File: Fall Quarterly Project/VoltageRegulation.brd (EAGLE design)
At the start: 160 x 100 mm, 24 parts, among them IC3 L272M

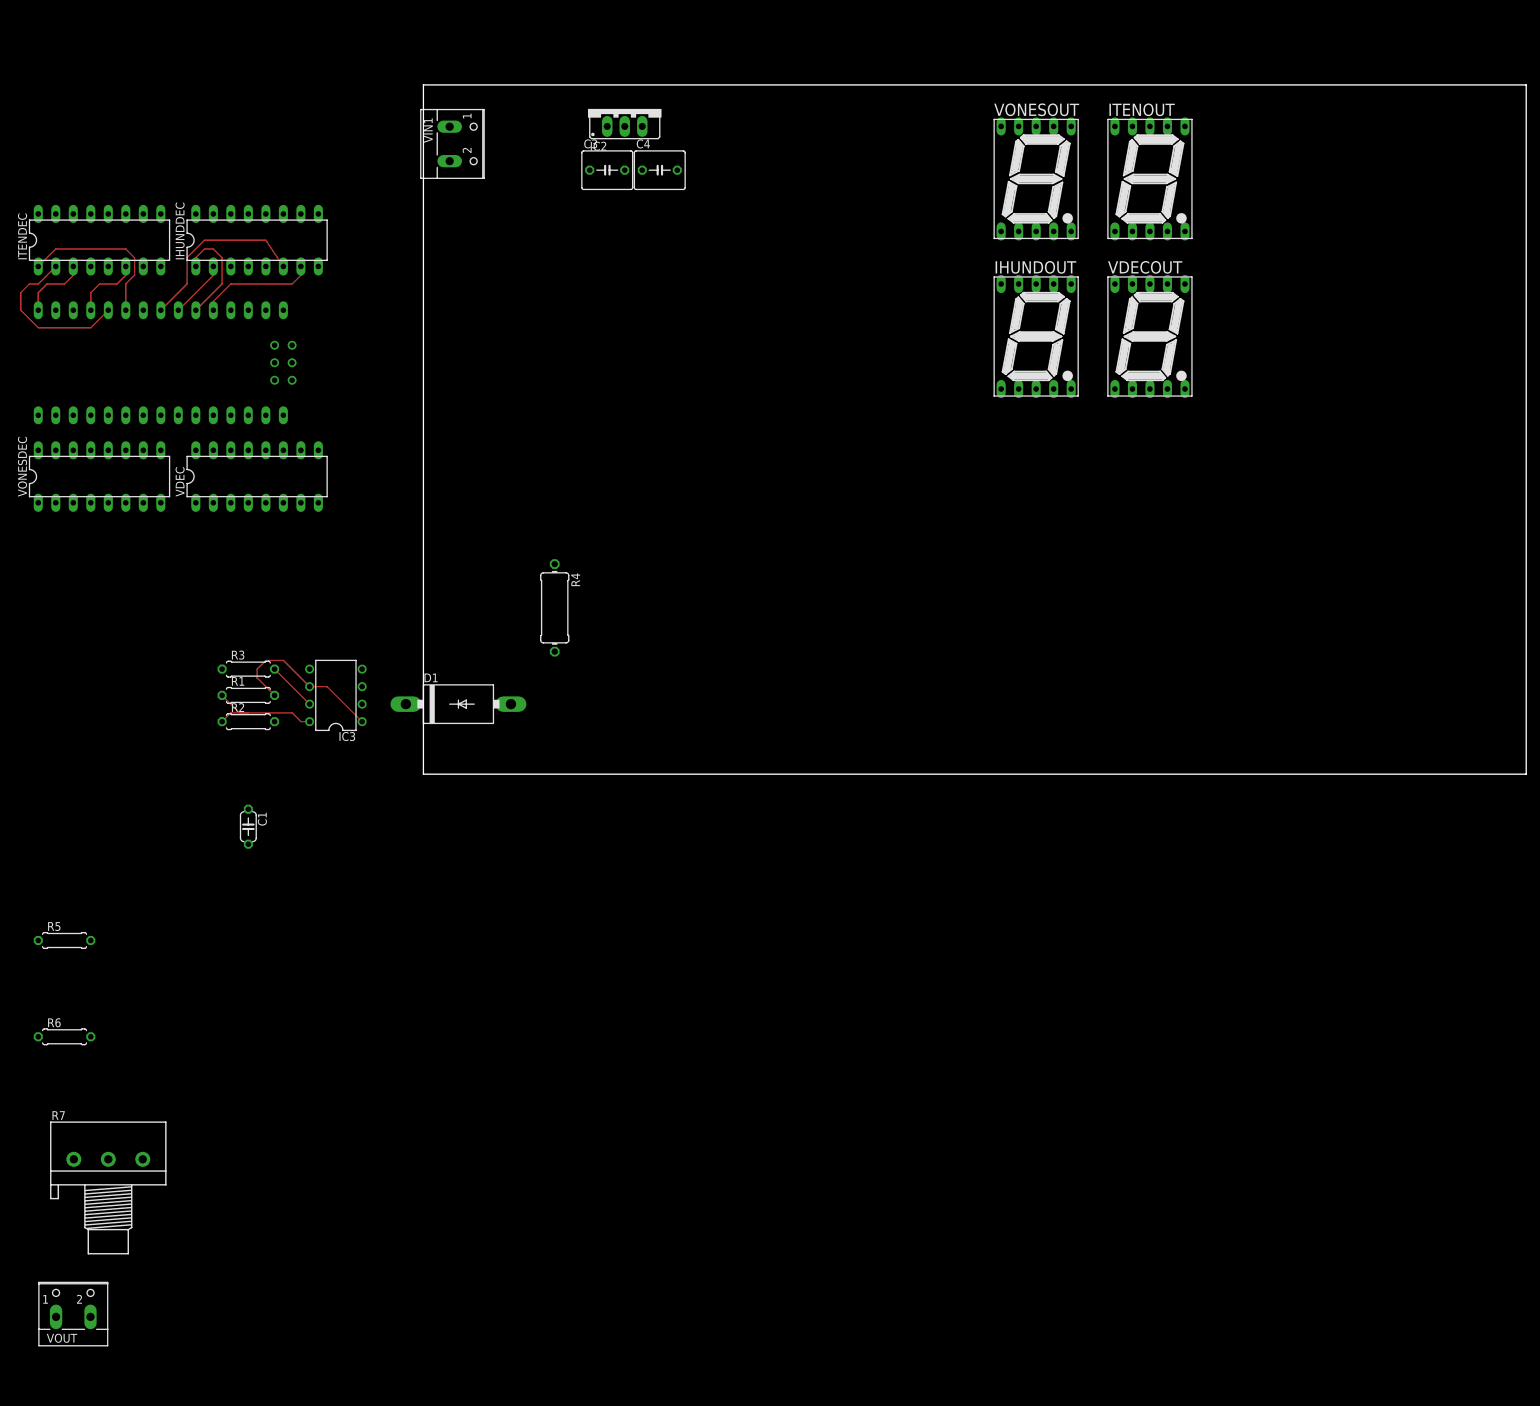
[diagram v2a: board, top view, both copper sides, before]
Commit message: Update 1.4
Just began routing the board and deciding where parts will lie. I'm keeping to one layer of the board for now, that way any nets that need to be escaped to another side of the board won't need any crazy routing to reach their destination.
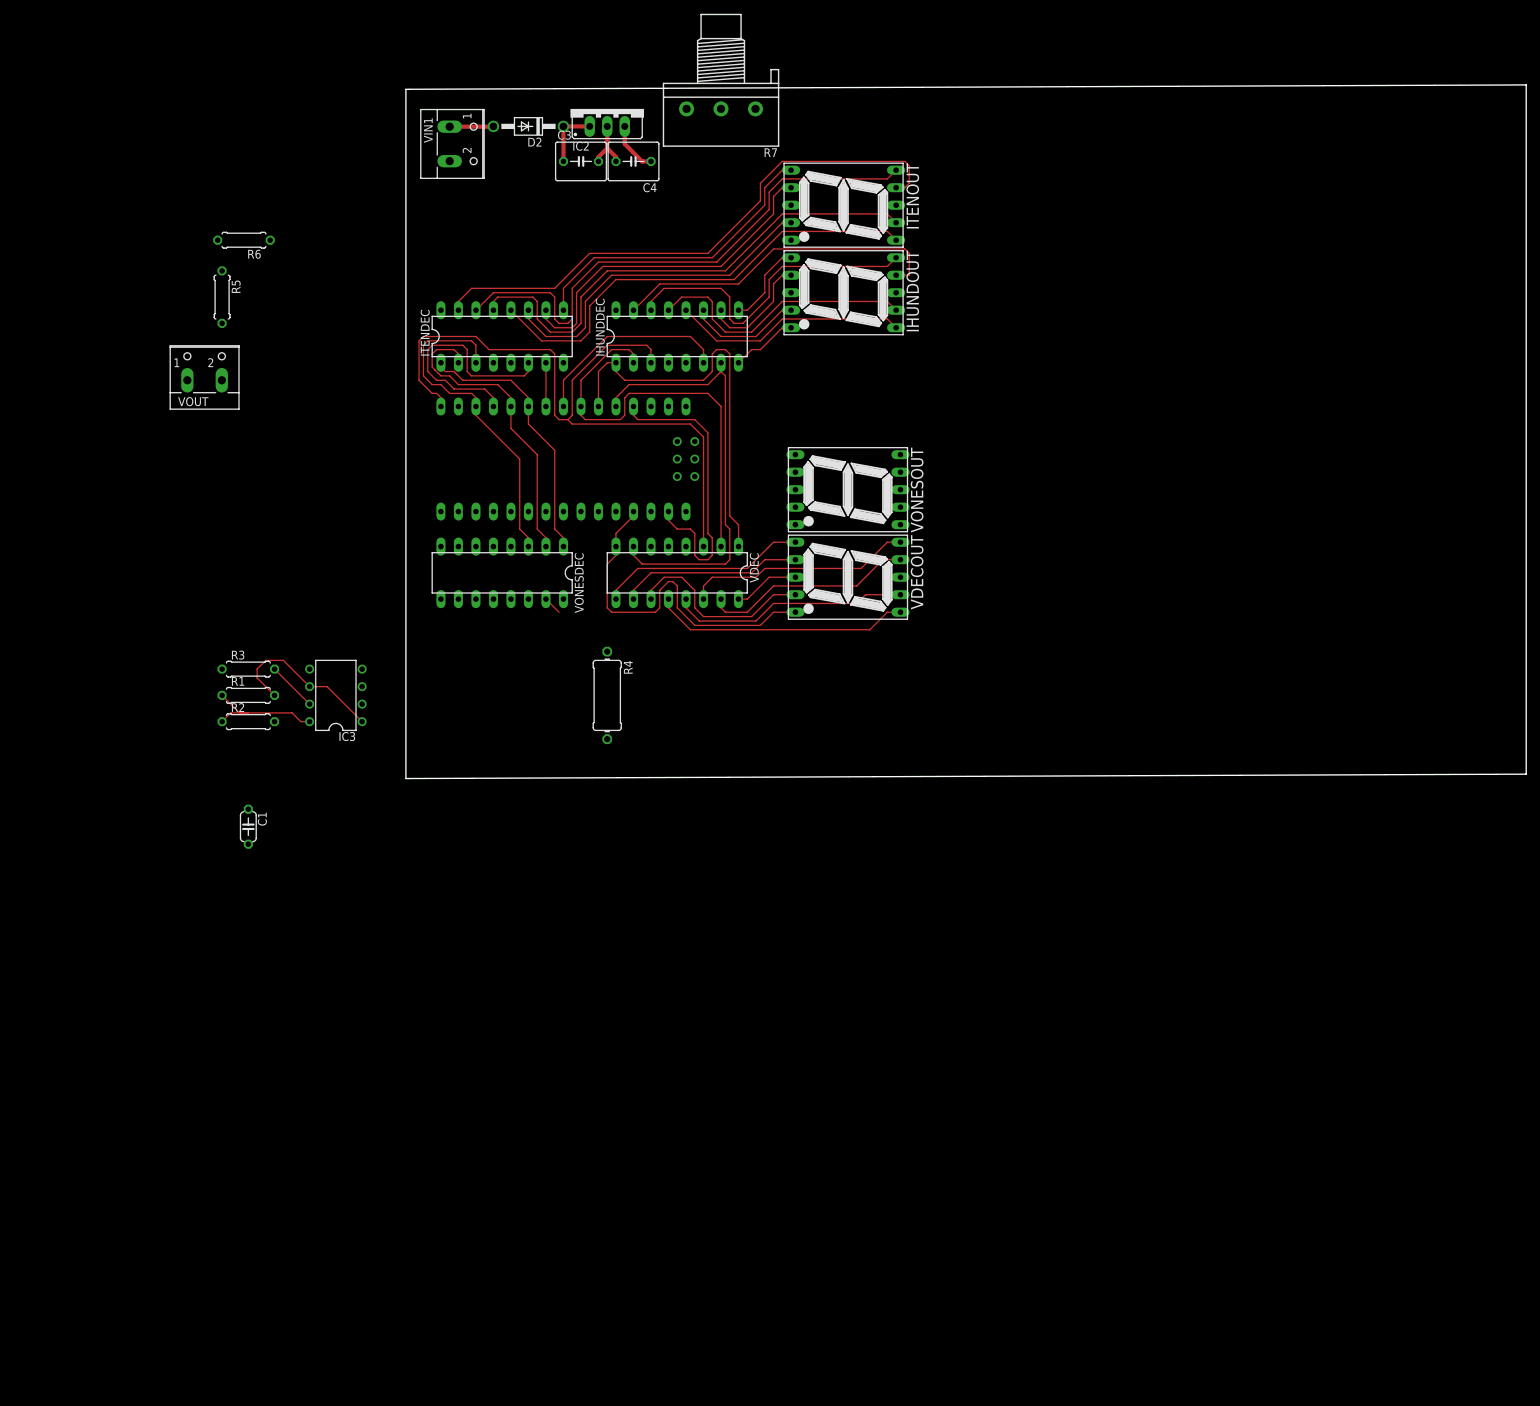
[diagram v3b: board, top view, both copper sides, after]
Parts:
- removed D1: SB320, diode:DO201-15
- added D2: 1N4004, diode:DO41-10
- moved R7 176.4 mm to (43.2, 96.5), turned to 180 degrees
- moved VOUT 137.2 mm to (-31.8, 58.4)
- moved R6 118.5 mm to (-26.0, 77.5), turned to 180 degrees
- moved R5 96.1 mm to (-29.2, 69.2), turned to 270 degrees
- moved IHUNDDEC 62.5 mm to (36.8, 63.5)
- moved VDEC 62.5 mm to (36.8, 29.2), turned to 180 degrees
- moved ITENDEC 60.1 mm to (11.4, 63.5)
- moved U$1 60.1 mm to (29.2, 48.3)
- moved VONESDEC 60.1 mm to (11.4, 29.2), turned to 180 degrees
- moved VDECOUT 56.0 mm to (61.6, 28.6), turned to 270 degrees
- moved VONESOUT 52.7 mm to (61.6, 41.3), turned to 270 degrees
- moved ITENOUT 44.6 mm to (61.0, 82.5), turned to 270 degrees
- moved IHUNDOUT 28.7 mm to (61.0, 69.8), turned to 270 degrees
- moved R4 14.8 mm to (26.7, 11.4)
- moved C3 4.02 mm to (22.9, 88.9)
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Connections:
- removed net VDD: IHUNDDEC.16, ITENDEC.16, VDEC.16, VONESDEC.16
- removed net VSS: IHUNDDEC.8, ITENDEC.8, VDEC.8, VONESDEC.8
- net +12V: now also D2.C; no longer D1.C
- net +5V: now also IHUNDDEC.8, ITENDEC.8, VDEC.8, VONESDEC.8
- net 10SDIGIT5: no longer ITENDEC.3
- net 1SDIGIT5: now also ITENDEC.3
- net GND: now also IHUNDDEC.16, ITENDEC.16, VDEC.16, VONESDEC.16
- net N$3: now also D2.A; no longer D1.A
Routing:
- net 10SDIGIT5: track 9.94 -> 102.8 mm
- net ITENBUS6: track 0.00 -> 81.6 mm
- net ITENBUS7: track 0.00 -> 79.0 mm
- net ITENBUS1: track 0.00 -> 73.4 mm
- net +5V: track 0.00 -> 68.9 mm
- net ITENBUS2: track 0.00 -> 67.1 mm
- net GND: track 0.00 -> 60.9 mm
- net 10SDIGIT3: track 8.45 -> 60.8 mm
- net ITENBUS4: track 0.00 -> 49.9 mm
- net ITENBUS3: track 0.00 -> 49.5 mm
- net 1SDIGIT5: track 0.00 -> 49.4 mm
- net 4DIGIT6: track 0.00 -> 49.0 mm
- net 10SDIGIT1: track 16.8 -> 64.5 mm
- net 4DIGIT7: track 0.00 -> 47.0 mm
- net ITENBUS5: track 0.00 -> 44.8 mm
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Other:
- board size 160 x 100 mm -> 162.5 x 100.6 mm

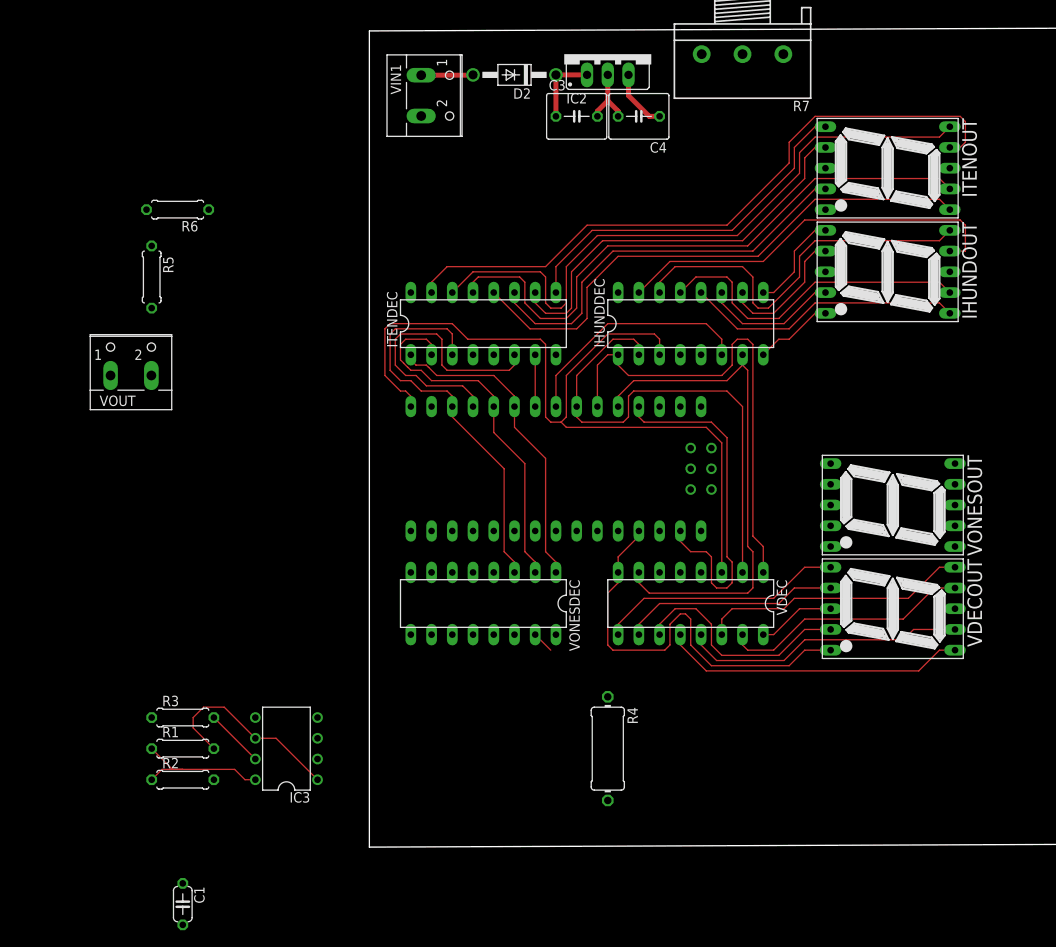
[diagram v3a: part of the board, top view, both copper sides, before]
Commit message: Update 1.5
More routing of signals, power traces went down and better organization of support circuitry
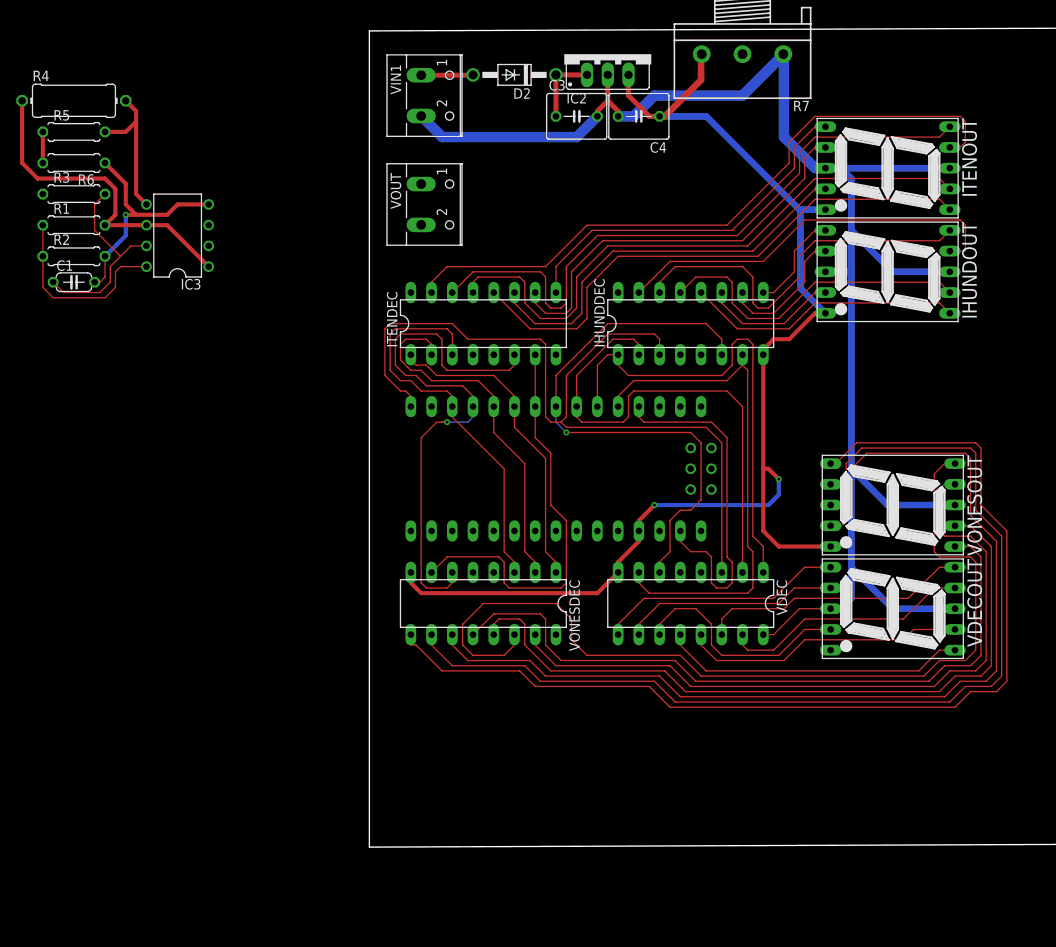
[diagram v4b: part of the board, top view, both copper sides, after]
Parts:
- moved R4 102.9 mm to (-38.7, 90.8), turned to 0 degrees
- moved C1 77.4 mm to (-38.7, 68.6), turned to 0 degrees
- moved R3 65.5 mm to (-38.7, 79.4)
- moved R1 65.5 mm to (-38.7, 75.6)
- moved R2 65.5 mm to (-38.7, 71.8)
- moved IC3 64.3 mm to (-26.0, 74.3)
- moved VOUT 41.8 mm to (5.08, 78.1), turned to 270 degrees
- moved R5 20.2 mm to (-38.7, 87.0), turned to 0 degrees
- moved R6 13.9 mm to (-38.7, 83.2)
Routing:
- net GND: track 60.9 -> 274.9 mm, vias 0 -> 1
- net 1DIGITBUS5: track 0.00 -> 128.4 mm
- net 1DIGITBUS4: track 0.00 -> 124.9 mm
- net 1DIGITBUS3: track 0.00 -> 123.7 mm
- net 1DIGITBUS7: track 0.00 -> 110.6 mm
- net 1DIGITBUS1: track 0.00 -> 89.1 mm
- net +5V: track 68.9 -> 155.7 mm, vias 0 -> 2
- net 1DIGITBUS2: track 0.00 -> 85.6 mm
- net 1DIGITBUS6: track 2.69 -> 87.3 mm
- net 1SDIGIT1: track 6.35 -> 50.1 mm
- net 10SDIGIT4: track 29.5 -> 69.0 mm, vias 0 -> 1
- net 1SDIGIT4: track 35.7 -> 67.7 mm, vias 0 -> 1
- net N$6: track 0.00 -> 18.1 mm
- net N$5: track 7.18 -> 24.9 mm
- net N$2: track 24.3 -> 40.1 mm
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
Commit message: Update 1.5
Finished routing board, needs work still confirming parts and ensuring layout and schematic are good.
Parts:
- moved R6 118.6 mm to (76.8, 56.5), turned to 270 degrees
- moved R5 117.1 mm to (74.3, 56.5), turned to 90 degrees
- moved R4 114.7 mm to (74.3, 71.1), turned to 90 degrees
- moved C1 107.0 mm to (67.9, 60.3)
- moved R1 98.9 mm to (57.8, 54.0)
- moved R2 98.9 mm to (57.8, 50.2)
- moved R3 98.9 mm to (57.8, 57.8)
- moved IC3 96.8 mm to (68.6, 54.0)
- moved VOUT 59.9 mm to (62.2, 95.9), turned to 0 degrees
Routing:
- net +12V: track 8.89 -> 105.2 mm
- net GND: track 274.9 -> 369.6 mm
- net N$10: track 0.00 -> 83.5 mm, vias 0 -> 2
- net N$9: track 0.00 -> 80.7 mm, vias 0 -> 2
- net N$7: track 3.81 -> 74.6 mm, vias 0 -> 2
- net N$1: track 0.00 -> 58.9 mm
- net +5V: track 155.7 -> 206.4 mm
- net N$6: track 18.1 -> 58.5 mm
- net N$5: track 24.9 -> 11.3 mm
- net N$4: track 23.5 -> 15.1 mm
- net N$2: track 40.1 -> 44.2 mm
- net 1DIGITBUS3: track 123.7 -> 120.3 mm
- net 1SDIGIT2: track 38.9 -> 40.0 mm
- net 1DIGITBUS4: track 124.9 -> 123.8 mm
- net 1SDIGIT3: track 44.5 -> 45.2 mm
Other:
- board size 162.5 x 100.6 mm -> 82.6 x 84.8 mm

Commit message: Update 1.6
Fixed current sense circuit, just need to update the board layout now
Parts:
- removed R4: (no value), rcl:0411/12
- added R10: 200, rcl:0207/7
- added R11: 100k, rcl:0207/7
- added R8: 0.02, rcl:0411/12
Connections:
- new net N$13: IC3.5, R10.2, R11.2
- net GND: now also R10.1, R8.1; no longer VOUT.1
- net N$10: now also R11.1
- net N$2: now also R8.2, VOUT.1; no longer IC3.1, R1.2, R4.1
- net N$6: now also IC3.1, R1.2; no longer IC3.5, R4.2
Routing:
- net N$10: track 83.5 -> 0.00 mm, vias 2 -> 0
- net N$2: track 44.2 -> 0.00 mm
- net N$6: track 58.5 -> 72.3 mm
- net N$14: track 74.6 -> 70.2 mm
- net GND: track 369.6 -> 366.9 mm
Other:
- board text added: "CPP IEEE FALL QUARTERLY PROJECT ZACHARY SQUIER"
